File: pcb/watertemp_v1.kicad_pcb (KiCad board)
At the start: 2 copper layers, 56 x 90 mm, 61 parts, among them J1 RN2483 Ext, J2 SWD, J3 I2C, J4 UART1, J5 UART0, Q1 Q_PMOS_GSD, Q2 Q_DUAL_NMOS_GSD_PMOS_SGD, U1 LPC11U24FBD48, U2 RN2483, U3 SHT21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

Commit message: Improve fabrication layer
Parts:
- R10: value 9.30K 0.1% -> 9.30K
- R9: value 6.04K 0.1% -> 6.04K
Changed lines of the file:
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@@
     (links 136)
     (no_connects 0)
-    (area 26.924999 39.924999 83.075001 130.075001)
+    (area 22.966905 37.719 91.100001 131.826001)
     (thickness 1.6)
     (drawings 32)
@@
   )
   (layers
-    (0 F.Cu signal)
-    (31 B.Cu signal)
-    (32 B.Adhes user)
+    (0 F.Cu signal hide)
+    (31 B.Cu signal hide)
+    (32 B.Adhes user hide)
     (33 F.Adhes user)
-    (34 B.Paste user)
-    (35 F.Paste user)
-    (36 B.SilkS user)
+    (34 B.Paste user hide)
+    (35 F.Paste user hide)
+    (36 B.SilkS user hide)
     (37 F.SilkS user)
-    (38 B.Mask user)
-    (39 F.Mask user)
+    (38 B.Mask user hide)
+    (39 F.Mask user hide)
     (40 Dwgs.User user hide)
-    (41 Cmts.User user)
-    (42 Eco1.User user)
-    (43 Eco2.User user)
+    (41 Cmts.User user hide)
+    (42 Eco1.User user hide)
+    (43 Eco2.User user hide)
     (44 Edge.Cuts user)
-    (45 Margin user)
-    (46 B.CrtYd user)
+    (45 Margin user hide)
+    (46 B.CrtYd user hide)
     (47 F.CrtYd user)
-    (48 B.Fab user)
+    (48 B.Fab user hide)
     (49 F.Fab user)
   )
@@
       (effects (font (size 0.8 0.8) (thickness 0.15)))
     )
-    (fp_text value "6.04K 0.1%" (at 0 1.75 270) (layer F.Fab)
+    (fp_text value 6.04K (at 0.1022 -1.46 270) (layer F.Fab)
       (effects (font (size 0.6 0.6) (thickness 0.08)))
     )
@@
       (effects (font (size 0.8 0.8) (thickness 0.15)))
     )
-    (fp_text value "RN2483 Ext" (at 0 17.57 270) (layer F.Fab)
+    (fp_text value "RN2483 Ext" (at -1.882 6.946 360) (layer F.Fab)
       (effects (font (size 1 1) (thickness 0.15)))
     )
@@
       (effects (font (size 0.8 0.8) (thickness 0.15)))
     )
-    (fp_text value LPC11U24FBD48 (at 0 6) (layer F.Fab)
+    (fp_text value LPC11U24FBD48 (at 6.622 -0.246 90) (layer F.Fab)
       (effects (font (size 1 1) (thickness 0.15)))
     )
@@
     (fp_line (start 1.8 4.35) (end 1.8 -1.8) (layer F.CrtYd) (width 0.05))
     (fp_line (start 1.8 -1.8) (end -1.8 -1.8) (layer F.CrtYd) (width 0.05))
-    (fp_text user %R (at 0 1.27 90) (layer F.Fab)
+    (fp_text user %R (at 2.7 1.27 90) (layer F.Fab)
       (effects (font (size 1 1) (thickness 0.15)))
     )
@@
     (fp_line (start 1.8 4.35) (end 1.8 -1.8) (layer F.CrtYd) (width 0.05))
     (fp_line (start 1.8 -1.8) (end -1.8 -1.8) (layer F.CrtYd) (width 0.05))
-    (fp_text user %R (at 0 1.27 90) (layer F.Fab)
+    (fp_text user %R (at 2.554 1.27 90) (layer F.Fab)
       (effects (font (size 1 1) (thickness 0.15)))
     )
@@
       (effects (font (size 0.8 0.8) (thickness 0.15)))
     )
-    (fp_text value 100nF (at -3.2004 0.4826) (layer F.Fab)
+    (fp_text value 100nF (at 0.166 1.652) (layer F.Fab)
       (effects (font (size 0.6 0.6) (thickness 0.1)))
     )
@@
       (effects (font (size 0.8 0.8) (thickness 0.15)))
     )
-    (fp_text value 100nF (at 0 1.75 90) (layer F.Fab)
-      (effects (font (size 1 1) (thickness 0.15)))
+    (fp_text value 100nF (at -2.214 1.615 270) (layer F.Fab)
+      (effects (font (size 0.6 0.6) (thickness 0.1)))
     )
     (fp_text user %R (at 0 -1.5 90) (layer F.Fab) hide
@@
       (effects (font (size 0.8 0.8) (thickness 0.15)))
     )
-    (fp_text value 10KΩ (at 0 1.75 270) (layer F.Fab)
-      (effects (font (size 1 1) (thickness 0.15)))
+    (fp_text value 10KΩ (at -2.335 -1.615 270) (layer F.Fab)
+      (effects (font (size 0.6 0.6) (thickness 0.1)))
     )
     (fp_text user %R (at 0 0 360) (layer F.Fab)
@@
       (effects (font (size 0.8 0.8) (thickness 0.15)))
     )
-    (fp_text value 10KΩ (at 0 1.75) (layer F.Fab)
-      (effects (font (size 1 1) (thickness 0.15)))
+    (fp_text value 10KΩ (at -1.991 -1.584) (layer F.Fab)
+      (effects (font (size 0.6 0.6) (thickness 0.1)))
     )
     (fp_text user %R (at 0 0) (layer F.Fab)
@@
       (effects (font (size 1 1) (thickness 0.15)))
     )
-    (fp_text value Antenna_Shield (at 3.53834 6.38032 270) (layer F.Fab)
+    (fp_text value Antenna_Shield (at -0.0375 6.38032 270) (layer F.Fab)
       (effects (font (size 1 1) (thickness 0.15)))
     )
@@
       (effects (font (size 0.8 0.8) (thickness 0.15)))
     )
-    (fp_text value Q_DUAL_NMOS_GSD_PMOS_SGD (at 2.3036 2.5502 90) (layer F.Fab)
+    (fp_text value Q_DUAL_NMOS_GSD_PMOS_SGD (at -0.2872 -1.7808 180) (layer F.Fab)
       (effects (font (size 0.4 0.4) (thickness 0.08)))
     )
@@
       (effects (font (size 0.8 0.8) (thickness 0.15)))
     )
-    (fp_text value "9.30K 0.1%" (at 2.159 -1.6256 270) (layer F.Fab)
+    (fp_text value 9.30K (at 0.163 -1.4346 270) (layer F.Fab)
       (effects (font (size 0.6 0.6) (thickness 0.08)))
     )
@@
       (effects (font (size 0.8 0.8) (thickness 0.15)))
     )
-    (fp_text value 10KΩ (at -0.0914 -1.7526 180) (layer F.Fab)
+    (fp_text value 10KΩ (at -0.6152 1.0798 180) (layer F.Fab)
       (effects (font (size 0.6 0.6) (thickness 0.1)))
     )
@@
       (effects (font (size 0.8 0.8) (thickness 0.15)))
     )
-    (fp_text value 10KΩ (at 0.08 -1.778 270) (layer F.Fab)
+    (fp_text value 10KΩ (at -3.723 -0.139 270) (layer F.Fab)
       (effects (font (size 1 1) (thickness 0.15)))
     )
@@
       (effects (font (size 0.8 0.8) (thickness 0.15)))
     )
-    (fp_text value 10KΩ (at 0 1.75 90) (layer F.Fab)
+    (fp_text value 10KΩ (at -3.783 0.139 90) (layer F.Fab)
       (effects (font (size 1 1) (thickness 0.15)))
     )
@@
       (effects (font (size 0.8 0.8) (thickness 0.15)))
     )
-    (fp_text value 470Ω (at -2.9464 0.7366 180) (layer F.Fab)
+    (fp_text value 470Ω (at -2.9464 -0.096 180) (layer F.Fab)
       (effects (font (size 0.6 0.6) (thickness 0.1)))
     )
@@
       (effects (font (size 0.8 0.8) (thickness 0.15)))
     )
-    (fp_text value 470Ω (at -3.001 -0.8128 180) (layer F.Fab)
+    (fp_text value 470Ω (at -3.001 -0.286 180) (layer F.Fab)
       (effects (font (size 0.6 0.6) (thickness 0.1)))
     )
@@
       (effects (font (size 0.8 0.8) (thickness 0.15)))
     )
-    (fp_text value 470Ω (at -2.3838 -1.8034 180) (layer F.Fab)
+    (fp_text value 470Ω (at -2.995 0.024 180) (layer F.Fab)
       (effects (font (size 0.6 0.6) (thickness 0.1)))
     )
@@
       (effects (font (size 0.8 0.8) (thickness 0.15)))
     )
-    (fp_text value 4.7K (at 0 1.75 270) (layer F.Fab)
-      (effects (font (size 1 1) (thickness 0.15)))
+    (fp_text value 4.7K (at 0 2.861 270) (layer F.Fab)
+      (effects (font (size 0.6 0.6) (thickness 0.1)))
     )
     (fp_text user %R (at 0 0 270) (layer F.Fab)
@@
       (effects (font (size 0.8 0.8) (thickness 0.15)))
     )
-    (fp_text value 1uF (at 1.4224 1.3208 270) (layer F.Fab)
+    (fp_text value 1uF (at -0.062 1.3208 270) (layer F.Fab)
       (effects (font (size 0.6 0.6) (thickness 0.1)))
     )
@@
       (effects (font (size 0.8 0.8) (thickness 0.15)))
     )
-    (fp_text value 1uF (at 1.159 -1.9812 270) (layer F.Fab)
+    (fp_text value 1uF (at -0.046 -1.485 270) (layer F.Fab)
       (effects (font (size 0.6 0.6) (thickness 0.1)))
     )

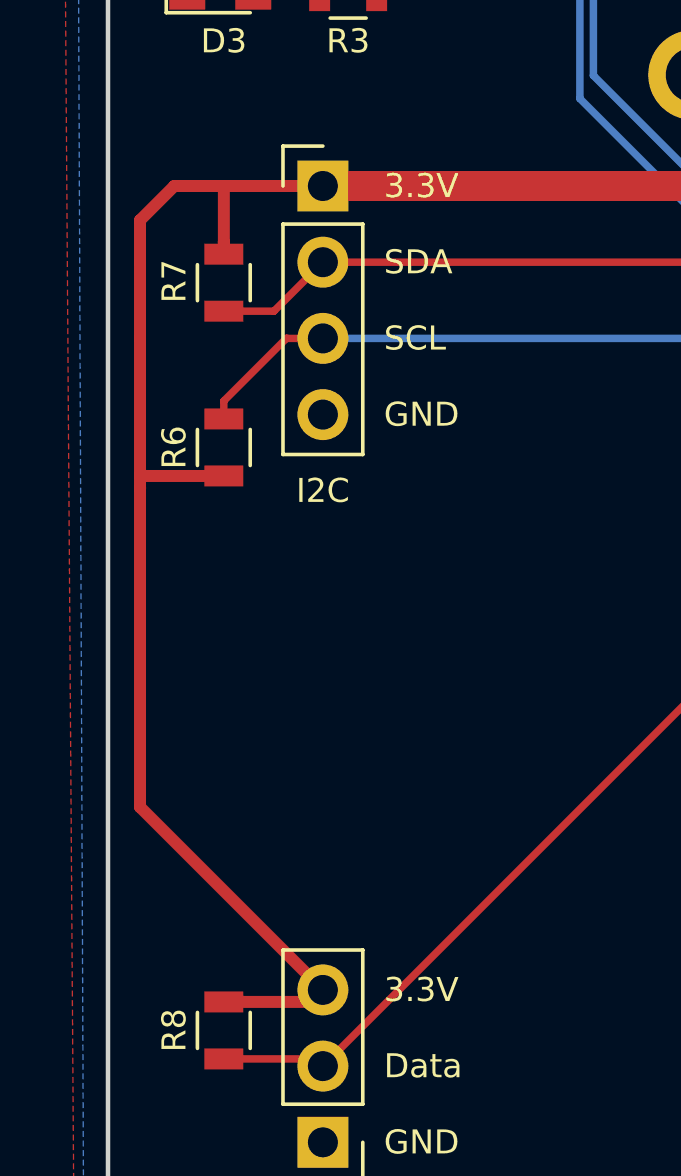
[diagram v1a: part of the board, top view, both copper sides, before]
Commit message: Improve R6/R7 placing
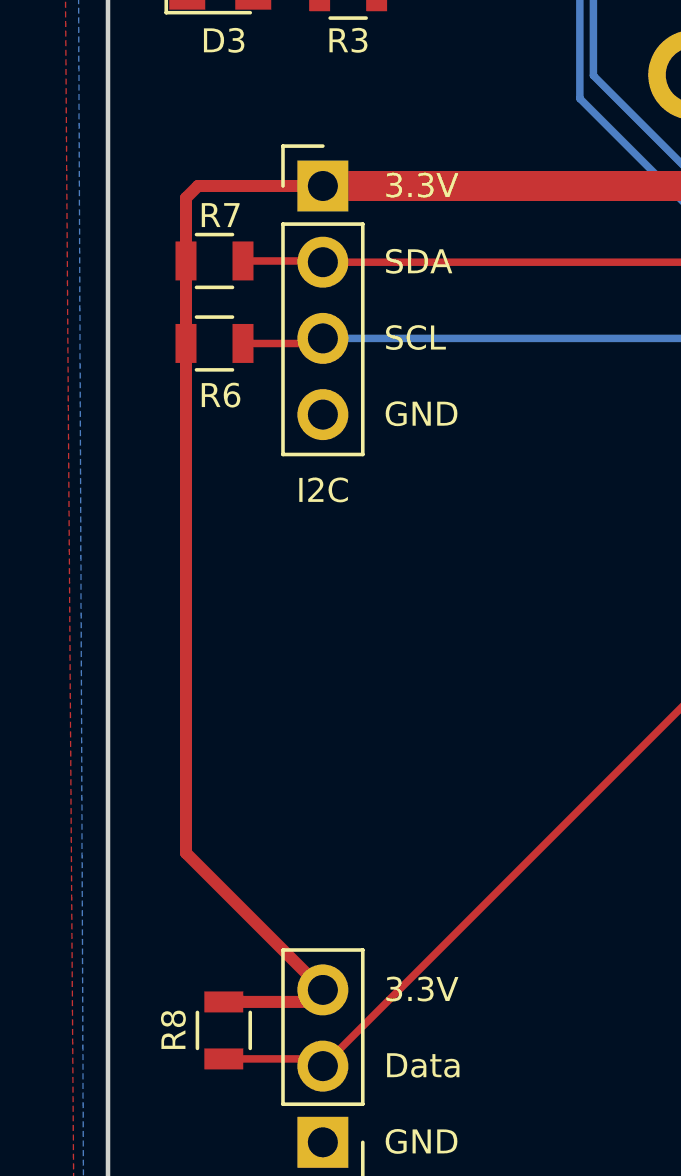
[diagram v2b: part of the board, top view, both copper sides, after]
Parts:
- moved R6 3.48 mm to (30.6, 76.8), turned to 0 degrees
- moved R7 0.79 mm to (30.6, 74.0), turned to 0 degrees
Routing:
- net 3.3V: track 238.4 -> 231.6 mm
- net SCL: track 122.4 -> 120.0 mm
- net SDA: track 115.6 -> 114.0 mm
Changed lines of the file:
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@@
     (thickness 1.6)
     (drawings 32)
-    (tracks 409)
+    (tracks 400)
     (zones 0)
     (modules 61)
@@
   )
   (layers
-    (0 F.Cu signal hide)
-    (31 B.Cu signal hide)
-    (32 B.Adhes user hide)
+    (0 F.Cu signal)
+    (31 B.Cu signal)
+    (32 B.Adhes user)
     (33 F.Adhes user)
-    (34 B.Paste user hide)
-    (35 F.Paste user hide)
+    (34 B.Paste user)
+    (35 F.Paste user)
     (36 B.SilkS user hide)
     (37 F.SilkS user)
-    (38 B.Mask user hide)
+    (38 B.Mask user)
     (39 F.Mask user hide)
-    (40 Dwgs.User user hide)
-    (41 Cmts.User user hide)
-    (42 Eco1.User user hide)
-    (43 Eco2.User user hide)
+    (40 Dwgs.User user)
+    (41 Cmts.User user)
+    (42 Eco1.User user)
+    (43 Eco2.User user)
     (44 Edge.Cuts user)
-    (45 Margin user hide)
-    (46 B.CrtYd user hide)
+    (45 Margin user)
+    (46 B.CrtYd user)
     (47 F.CrtYd user)
-    (48 B.Fab user hide)
+    (48 B.Fab user)
     (49 F.Fab user)
   )
@@
   )
   (module Resistors_SMD:R_0805 (layer F.Cu)
-    (at 30.861 74.723 270)
+    (at 30.55 74)
     (descr "Resistor SMD 0805, reflow soldering, Vishay (see dcrcw.pdf)")
     (tags "resistor 0805")
     (attr smd)
-    (fp_text reference R7 (at -0.047 1.651 270) (layer F.SilkS)
+    (fp_text reference R7 (at 0.2 -1.5) (layer F.SilkS)
       (effects (font (size 0.8 0.8) (thickness 0.15)))
     )
-    (fp_text value 10KΩ (at -3.723 -0.139 270) (layer F.Fab)
-      (effects (font (size 1 1) (thickness 0.15)))
+    (fp_text value 10KΩ (at -2.111 0 90) (layer F.Fab)
+      (effects (font (size 0.6 0.6) (thickness 0.1)))
     )
-    (fp_text user %R (at 0 0 270) (layer F.Fab)
+    (fp_text user %R (at 0 0) (layer F.Fab)
       (effects (font (size 0.5 0.5) (thickness 0.075)))
     )
@@
     (fp_line (start 1.55 0.9) (end 1.55 -0.9) (layer F.CrtYd) (width 0.05))
     (fp_line (start 1.55 0.9) (end -1.55 0.9) (layer F.CrtYd) (width 0.05))
-    (pad 1 smd rect (at -0.95 0 270) (size 0.7 1.3) (layers F.Cu F.Paste F.Mask)
+    (pad 1 smd rect (at -0.95 0) (size 0.7 1.3) (layers F.Cu F.Paste F.Mask)
       (net 6 3.3V))
-    (pad 2 smd rect (at 0.95 0 270) (size 0.7 1.3) (layers F.Cu F.Paste F.Mask)
+    (pad 2 smd rect (at 0.95 0) (size 0.7 1.3) (layers F.Cu F.Paste F.Mask)
       (net 15 SDA))
     (model ${KISYS3DMOD}/Resistors_SMD.3dshapes/R_0805.wrl
@@
   )
   (module Resistors_SMD:R_0805 (layer F.Cu)
-    (at 30.861 80.217 90)
+    (at 30.55 76.75)
     (descr "Resistor SMD 0805, reflow soldering, Vishay (see dcrcw.pdf)")
     (tags "resistor 0805")
     (attr smd)
-    (fp_text reference R6 (at 0.0038 -1.651 90) (layer F.SilkS)
+    (fp_text reference R6 (at 0.2 1.75) (layer F.SilkS)
       (effects (font (size 0.8 0.8) (thickness 0.15)))
     )
-    (fp_text value 10KΩ (at -3.783 0.139 90) (layer F.Fab)
-      (effects (font (size 1 1) (thickness 0.15)))
+    (fp_text value 10KΩ (at -2.111 0 90) (layer F.Fab)
+      (effects (font (size 0.6 0.6) (thickness 0.1)))
     )
-    (fp_text user %R (at 0 0 90) (layer F.Fab)
+    (fp_text user %R (at 0 0) (layer F.Fab)
       (effects (font (size 0.5 0.5) (thickness 0.075)))
     )
@@
     (fp_line (start 1.55 0.9) (end 1.55 -0.9) (layer F.CrtYd) (width 0.05))
     (fp_line (start 1.55 0.9) (end -1.55 0.9) (layer F.CrtYd) (width 0.05))
-    (pad 1 smd rect (at -0.95 0 90) (size 0.7 1.3) (layers F.Cu F.Paste F.Mask)
+    (pad 1 smd rect (at -0.95 0) (size 0.7 1.3) (layers F.Cu F.Paste F.Mask)
       (net 6 3.3V))
-    (pad 2 smd rect (at 0.95 0 90) (size 0.7 1.3) (layers F.Cu F.Paste F.Mask)
+    (pad 2 smd rect (at 0.95 0) (size 0.7 1.3) (layers F.Cu F.Paste F.Mask)
       (net 16 SCL))
     (model ${KISYS3DMOD}/Resistors_SMD.3dshapes/R_0805.wrl
@@
       (effects (font (size 0.8 0.8) (thickness 0.15)))
     )
-    (fp_text value 470Ω (at -3.001 -0.286 180) (layer F.Fab)
+    (fp_text value 470Ω (at -3.001 -0.036 180) (layer F.Fab)
       (effects (font (size 0.6 0.6) (thickness 0.1)))
     )
@@
   (segment (start 61.849 59.055) (end 61.849 58.023) (width 0.25) (layer F.Cu) (net 5))
   (segment (start 61.849 60.284) (end 61.849 59.055) (width 0.25) (layer F.Cu) (net 5))
+  (segment (start 34.163 71.501) (end 29.999 71.501) (width 0.4) (layer F.Cu) (net 6))
+  (segment (start 29.999 71.501) (end 29.6 71.9) (width 0.4) (layer F.Cu) (net 6))
+  (segment (start 29.6 71.9) (end 29.6 72.4) (width 0.4) (layer F.Cu) (net 6))
+  (segment (start 29.6 72.4) (end 29.6 74) (width 0.4) (layer F.Cu) (net 6))
+  (segment (start 29.6 76.75) (end 29.6 93.735) (width 0.4) (layer F.Cu) (net 6))
+  (segment (start 29.6 93.735) (end 34.163 98.298) (width 0.4) (layer F.Cu) (net 6))
+  (segment (start 29.6 74) (end 29.6 76.75) (width 0.4) (layer F.Cu) (net 6))
   (segment (start 77.2414 123.7488) (end 65.7352 123.7488) (width 0.4) (layer F.Cu) (net 6))
   (segment (start 65.7352 123.7488) (end 62.5221 126.9619) (width 0.4) (layer F.Cu) (net 6))
@@
   (via (at 67.8434 51.5366) (size 0.6) (drill 0.4) (layers F.Cu B.Cu) (net 6))
   (segment (start 67.834 53.848) (end 67.834 51.8922) (width 0.4) (layer F.Cu) (net 6))
-  (segment (start 30.861 71.501) (end 30.861 73.373) (width 0.4) (layer F.Cu) (net 6))
-  (segment (start 30.861 73.373) (end 30.861 73.773) (width 0.4) (layer F.Cu) (net 6))
-  (segment (start 28.067 76.581) (end 28.067 81.153) (width 0.4) (layer F.Cu) (net 6))
-  (segment (start 28.067 81.153) (end 28.067 81.5721) (width 0.4) (layer F.Cu) (net 6))
-  (segment (start 30.861 81.167) (end 28.081 81.167) (width 0.4) (layer F.Cu) (net 6))
-  (segment (start 28.081 81.167) (end 28.067 81.153) (width 0.4) (layer F.Cu) (net 6))
   (segment (start 69.85 44.45) (end 72.0598 44.45) (width 0.4) (layer F.Cu) (net 6))
   (segment (start 64.135 53.848) (end 66.548 53.848) (width 1) (layer F.Cu) (net 6))
@@
   (segment (start 66.548 53.848) (end 67.834 53.848) (width 1) (layer F.Cu) (net 6))
   (segment (start 34.0106 98.1456) (end 34.163 98.298) (width 0.4) (layer F.Cu) (net 6))
-  (segment (start 28.067 81.5721) (end 28.067 92.202) (width 0.4) (layer F.Cu) (net 6))
-  (segment (start 28.067 81.5721) (end 28.0721 81.567) (width 0.4) (layer F.Cu) (net 6))
-  (segment (start 34.163 71.501) (end 30.861 71.501) (width 0.4) (layer F.Cu) (net 6))
-  (segment (start 30.861 71.501) (end 29.21 71.501) (width 0.4) (layer F.Cu) (net 6))
   (segment (start 69.98208 58.709878) (end 69.98208 58.82132) (width 0.4) (layer B.Cu) (net 6))
   (segment (start 69.500201 58.227999) (end 69.98208 58.709878) (width 0.4) (layer B.Cu) (net 6))
@@
   (segment (start 80.2025 124.984) (end 80.3275 124.984) (width 0.4) (layer F.Cu) (net 6))
   (segment (start 78.9673 123.7488) (end 80.2025 124.984) (width 0.4) (layer F.Cu) (net 6))
-  (segment (start 28.067 92.202) (end 34.163 98.298) (width 0.4) (layer F.Cu) (net 6))
-  (segment (start 28.067 74.041) (end 28.067 76.581) (width 0.4) (layer F.Cu) (net 6))
-  (segment (start 28.067 72.644) (end 28.067 74.041) (width 0.4) (layer F.Cu) (net 6))
-  (segment (start 29.21 71.501) (end 28.067 72.644) (width 0.4) (layer F.Cu) (net 6))
   (segment (start 69.628 56.896) (end 69.628 55.767) (width 0.25) (layer F.Cu) (net 6))
   (segment (start 69.628 55.767) (end 67.834 53.973) (width 0.25) (layer F.Cu) (net 6))
@@
   (segment (start 75.9598 50.7862) (end 75.946 50.8) (width 0.25) (layer F.Cu) (net 14))
   (via (at 75.946 50.8) (size 0.6) (drill 0.4) (layers F.Cu B.Cu) (net 14))
+  (segment (start 31.811 74) (end 34.122 74) (width 0.25) (layer F.Cu) (net 15))
+  (segment (start 34.122 74) (end 34.163 74.041) (width 0.25) (layer F.Cu) (net 15))
   (segment (start 54.483 74.041) (end 54.483 74.0537) (width 0.25) (layer F.Cu) (net 15))
   (segment (start 54.957991 89.779731) (end 54.957991 122.324668) (width 0.25) (layer F.Cu) (net 15))
@@
   (segment (start 62.057302 67.691) (end 60.833 67.691) (width 0.25) (layer B.Cu) (net 15))
   (segment (start 60.833 67.691) (end 54.483 74.041) (width 0.25) (layer B.Cu) (net 15))
-  (segment (start 30.861 75.673) (end 32.531 75.673) (width 0.25) (layer F.Cu) (net 15))
-  (segment (start 32.531 75.673) (end 34.163 74.041) (width 0.25) (layer F.Cu) (net 15))
   (segment (start 69.128 67.6764) (end 69.1134 67.691) (width 0.25) (layer F.Cu) (net 15))
   (segment (start 69.128 65.596) (end 69.128 67.6764) (width 0.25) (layer F.Cu) (net 15))
@@
   (via (at 69.1134 67.691) (size 0.6) (drill 0.4) (layers F.Cu B.Cu) (net 15))
   (via (at 54.483 74.041) (size 0.6) (drill 0.4) (layers F.Cu B.Cu) (net 15))
-  (segment (start 30.861 79.267) (end 30.861 78.667) (width 0.25) (layer F.Cu) (net 16))
-  (segment (start 30.861 78.667) (end 32.947 76.581) (width 0.25) (layer F.Cu) (net 16))
-  (segment (start 32.947 76.581) (end 32.960919 76.581) (width 0.25) (layer F.Cu) (net 16))
-  (segment (start 32.960919 76.581) (end 34.163 76.581) (width 0.25) (layer F.Cu) (net 16))
+  (segment (start 31.811 76.75) (end 33.994 76.75) (width 0.25) (layer F.Cu) (net 16))
+  (segment (start 33.994 76.75) (end 34.163 76.581) (width 0.25) (layer F.Cu) (net 16))
   (segment (start 68.148198 67.7312) (end 68.148198 67.917146) (width 0.25) (layer F.Cu) (net 16))
   (segment (start 68.628 67.251398) (end 68.148198 67.7312) (width 0.25) (layer F.Cu) (net 16))
